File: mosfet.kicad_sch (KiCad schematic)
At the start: 11 parts, among them Q1 2N7002, Q2 IRF4905, Q3 IRF4905

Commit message: Reannotate everything
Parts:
- renumbered D1 to D3, D2 to D4, R4 to R10, R1 to R7, R2 to R8, R3 to R9
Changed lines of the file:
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@@
   (symbol (lib_id "power:GND") (at 128.905 118.11 0) (unit 1)
     (in_bom yes) (on_board yes)
-    (property "Reference" "#PWR02" (id 0) (at 128.905 124.46 0)
+    (property "Reference" "#PWR020" (id 0) (at 128.905 124.46 0)
       (effects (font (size 1.27 1.27)) hide)
     )
@@
   (symbol (lib_id "Device:R_Small") (at 128.905 90.805 0) (unit 1)
     (in_bom yes) (on_board yes) (fields_autoplaced)
-    (property "Reference" "R1" (id 0) (at 130.4036 89.9703 0)
+    (property "Reference" "R7" (id 0) (at 130.4036 89.9703 0)
       (effects (font (size 1.27 1.27)) (justify left))
     )
@@
   (symbol (lib_id "Device:R_Small") (at 128.905 104.14 0) (unit 1)
     (in_bom yes) (on_board yes) (fields_autoplaced)
-    (property "Reference" "R2" (id 0) (at 130.4036 103.3053 0)
+    (property "Reference" "R8" (id 0) (at 130.4036 103.3053 0)
       (effects (font (size 1.27 1.27)) (justify left))
     )
@@
   (symbol (lib_id "Device:R_Small") (at 149.225 93.98 180) (unit 1)
     (in_bom yes) (on_board yes) (fields_autoplaced)
-    (property "Reference" "R4" (id 0) (at 150.7236 93.1453 0)
+    (property "Reference" "R10" (id 0) (at 150.7236 93.1453 0)
       (effects (font (size 1.27 1.27)) (justify right))
     )
@@
   (symbol (lib_id "Diode:ZMMxx") (at 111.76 94.615 270) (unit 1)
     (in_bom yes) (on_board yes) (fields_autoplaced)
-    (property "Reference" "D2" (id 0) (at 113.792 93.7803 90)
+    (property "Reference" "D4" (id 0) (at 113.792 93.7803 90)
       (effects (font (size 1.27 1.27)) (justify left))
     )
@@
   (symbol (lib_id "Device:R_Small") (at 139.7 93.98 180) (unit 1)
     (in_bom yes) (on_board yes) (fields_autoplaced)
-    (property "Reference" "R3" (id 0) (at 141.1986 93.1453 0)
+    (property "Reference" "R9" (id 0) (at 141.1986 93.1453 0)
       (effects (font (size 1.27 1.27)) (justify right))
     )
@@
   (symbol (lib_id "Diode:ZMMxx") (at 111.76 87.63 270) (unit 1)
     (in_bom yes) (on_board yes) (fields_autoplaced)
-    (property "Reference" "D1" (id 0) (at 113.792 86.7953 90)
+    (property "Reference" "D3" (id 0) (at 113.792 86.7953 90)
       (effects (font (size 1.27 1.27)) (justify left))
     )

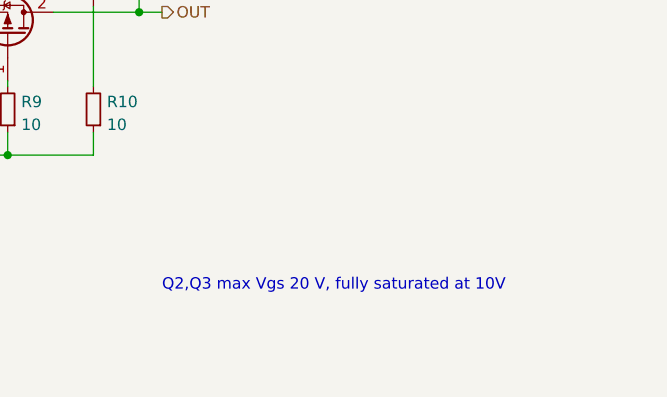
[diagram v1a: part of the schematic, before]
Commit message: Update label text in subsheet
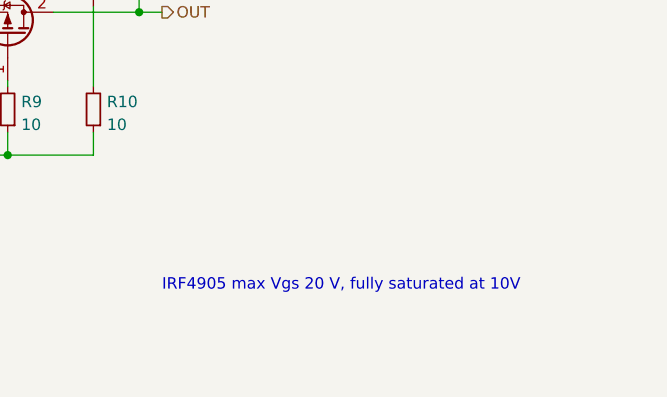
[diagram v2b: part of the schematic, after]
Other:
- note added: "IRF4905 max Vgs 20 V, fully saturated at 10V"
- note removed: "Q2,Q3 max Vgs 20 V, fully saturated at 10V"
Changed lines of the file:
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@@
     (stroke (width 0) (type default) (color 0 0 0 0))
   )
-  (text "Q2,Q3 max Vgs 20 V, fully saturated at 10V" (at 156.845 114.3 0)
+  (text "IRF4905 max Vgs 20 V, fully saturated at 10V" (at 156.845 114.3 0)
     (effects (font (size 1.27 1.27)) (justify left bottom))
   )

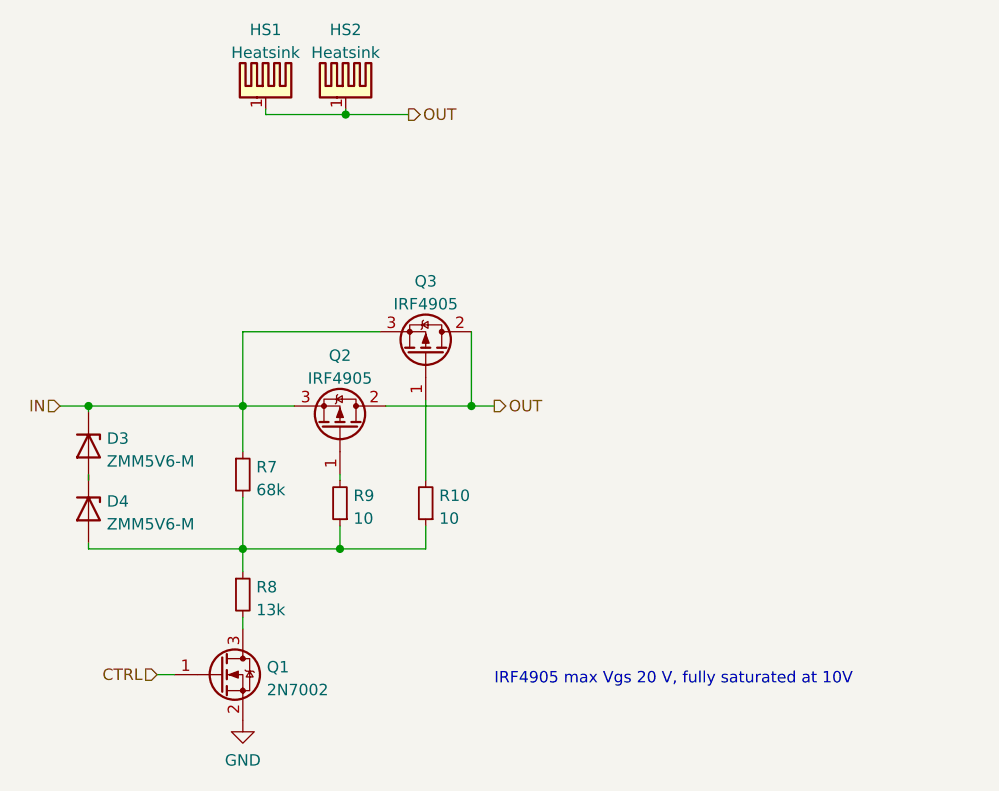
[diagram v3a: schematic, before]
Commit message: Mosfet drive clearances larger, update comments
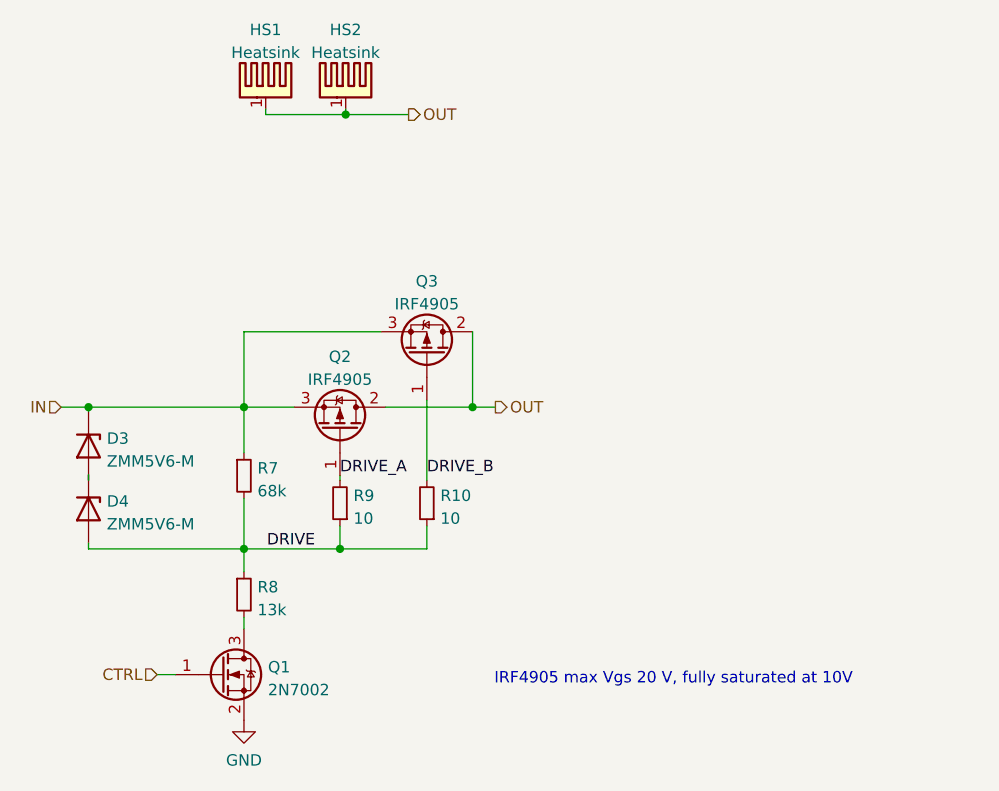
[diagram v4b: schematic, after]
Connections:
- net DRIVE: now reaches D4.2 (A), R10.1, R7.2, R8.1, R9.1
- net DRIVE_A: now reaches Q2.1 (G), R9.2
- net DRIVE_B: now reaches Q3.1 (G), R10.2
